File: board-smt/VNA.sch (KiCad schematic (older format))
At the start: 101 parts, among them J1 Conn_02x07_Odd_Even, J10 Conn_01x01, J11 Conn_01x01, J12 Conn_01x01, J13 Barrel_Jack, J14 Conn_01x01, J15 Conn_01x02, J16 Conn_01x01, J17 Conn_01x04, J18 Conn_01x01, J19 Conn_01x01, J2 Conn_Coaxial, J20 Conn_01x01, J21 Conn_01x01, J22 Conn_01x02, J24 USB_B, J3 Conn_01x01, J4 Conn_01x01, J5 Conn_01x01, J6 Conn_01x01, J7 Conn_01x01, J8 Conn_01x01, J9 Conn_Coaxial, Q3 S9018, SW1 SW_DPDT_x2, U1 SI5351A, U10 MT3608, U11 CN3052, U8 AMS1117-3V3, U9 78M05_TO252, Y1 27 MHz

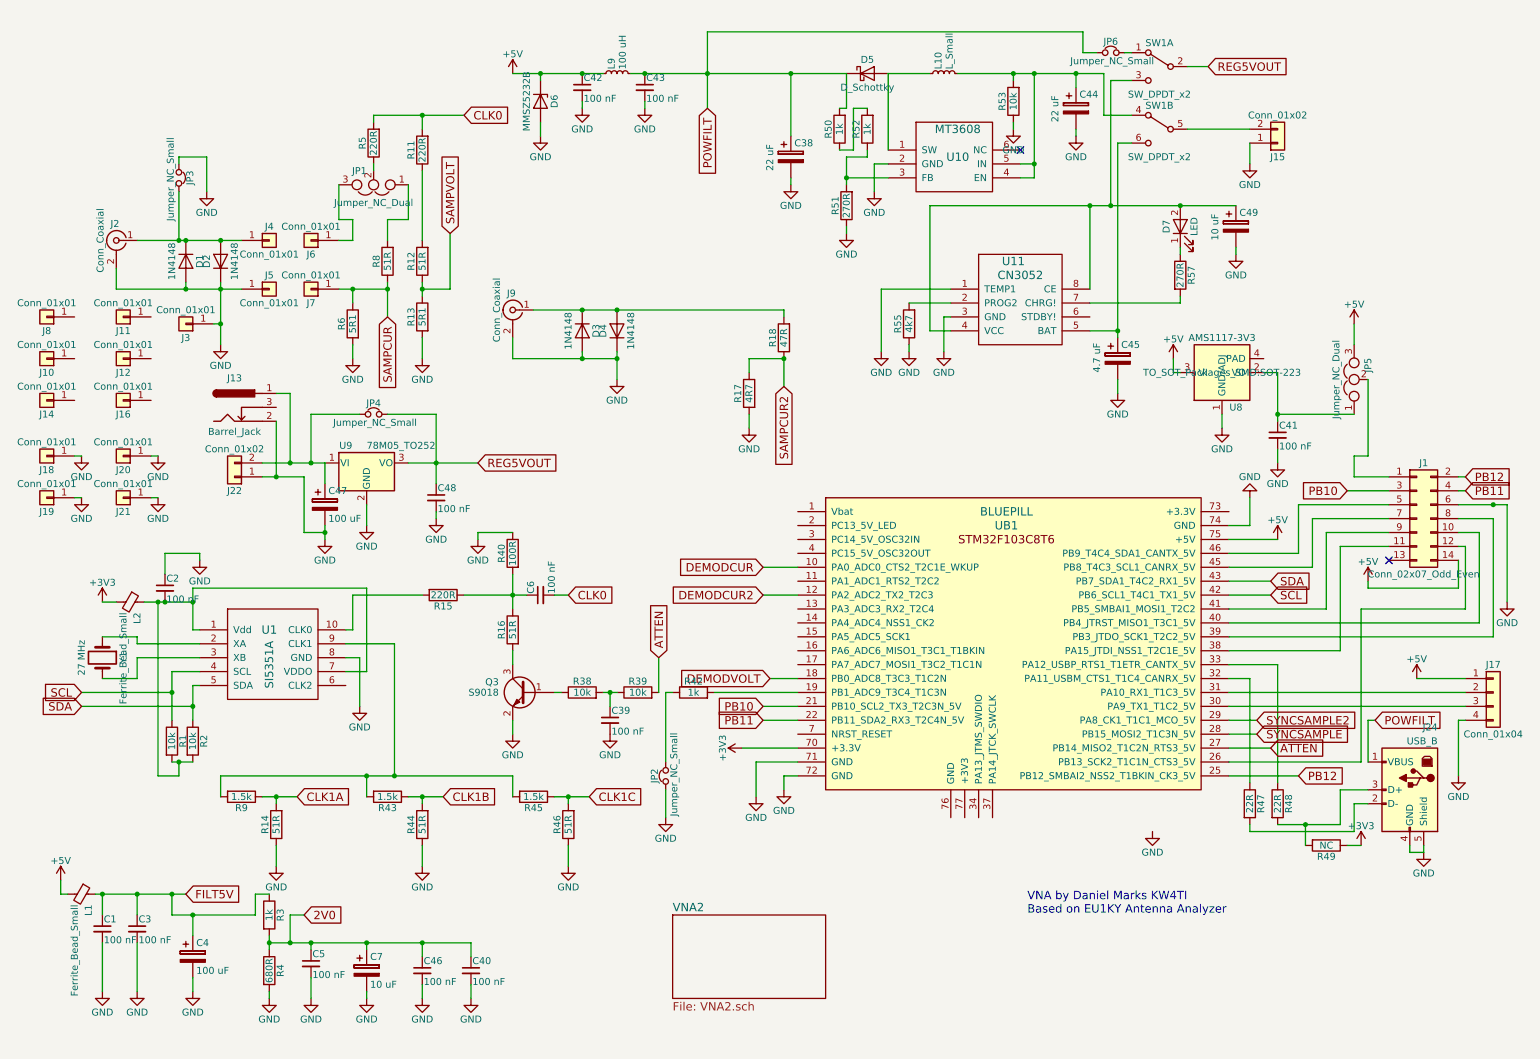
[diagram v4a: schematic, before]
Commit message: Added provision for separate SI5351A for LO signal
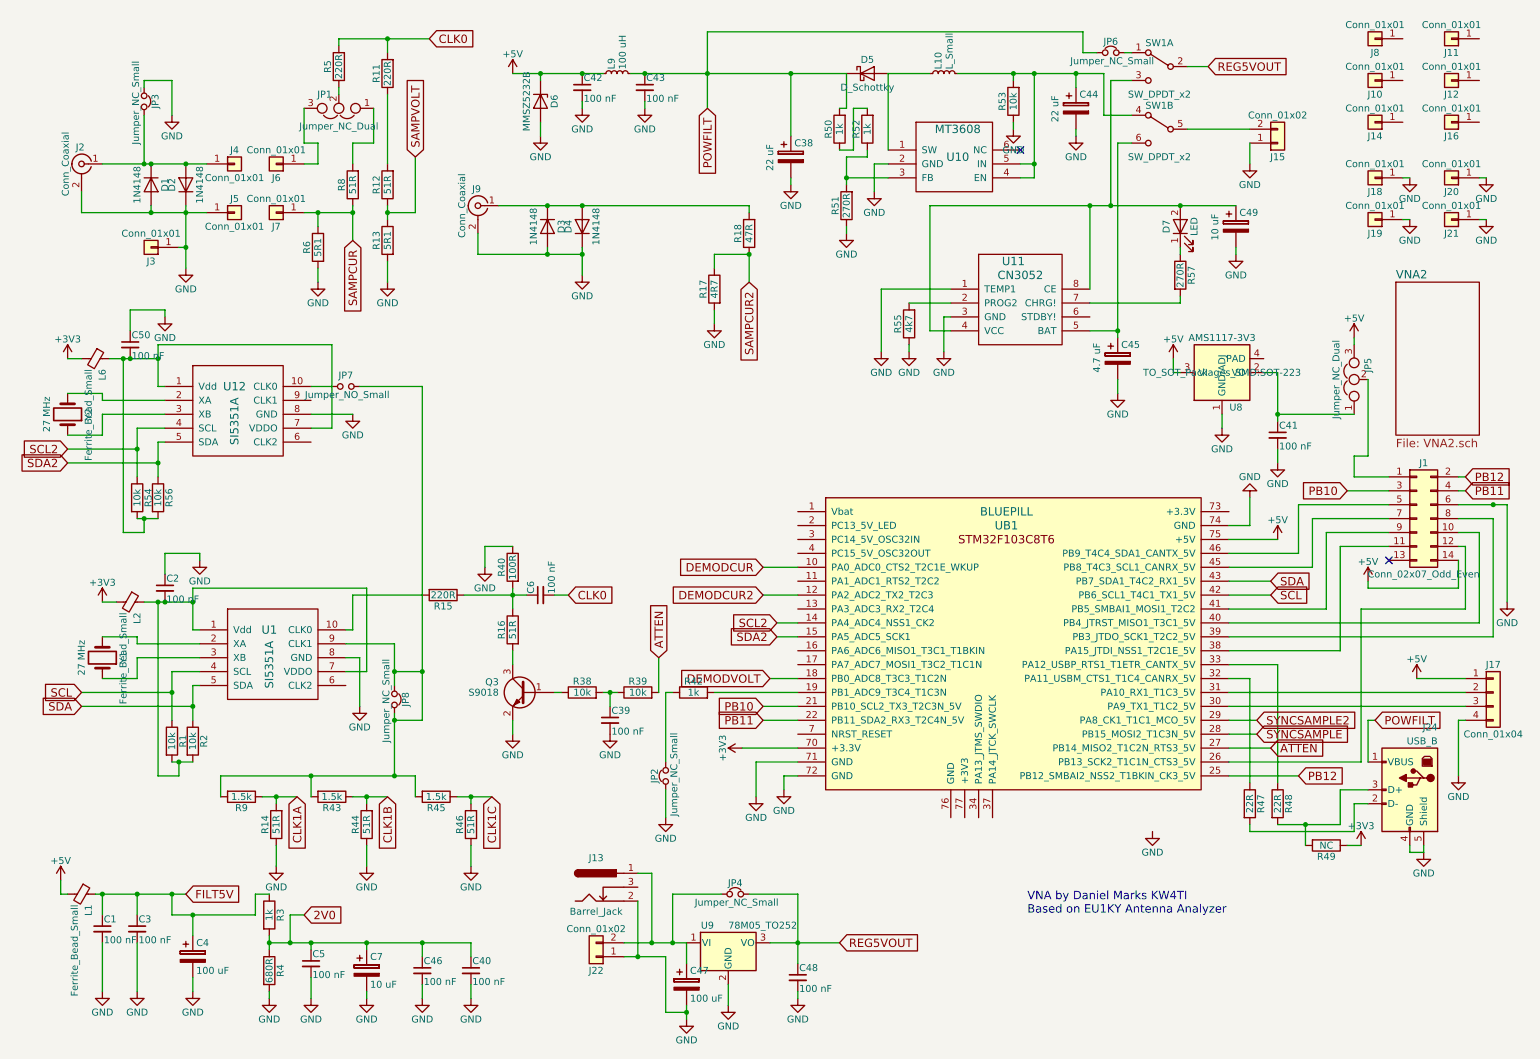
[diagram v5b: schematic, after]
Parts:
- added C50: 100 nF, Capacitors_SMD:C_0805_HandSoldering, symbol C_Small
- added JP7: Jumper_NO_Small, VNA:PAD_DEFAULT_OPEN, symbol Jumper_NO_Small
- added JP8: Jumper_NC_Small, VNA:PAD_DEFAULT_OPEN, symbol Jumper_NC_Small
- added L6: Ferrite_Bead_Small, Inductors_SMD:L_0805_HandSoldering, symbol Ferrite_Bead_Small
- added R54, R56: 10k, Resistors_SMD:R_0805_HandSoldering, symbol R
- added U12: SI5351A, Housings_SSOP:MSOP-10_3x3mm_Pitch0.5mm, symbol SI5351A
- added Y2: 27 MHz, Crystals:Crystal_SMD_3225-4pin_3.2x2.5mm_HandSoldering, symbol Crystal
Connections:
- net +3V3: now also L6.2
- net GND: now also C50.1, U12.8 (GND)
- net SCL2: now reaches UB1.14 (PA4_ADC4_NSS1_CK2)
- net SCL2: now also R54.1, U12.4 (SCL)
- net SDA2: now reaches UB1.15 (PA5_ADC5_SCK1)
- net SDA2: now also R56.1, U12.5 (SDA)
- net at U1.2 (XA): now also Y1.2; no longer Y1.1
- net at U1.3 (XB): now also Y1.1; no longer Y1.2
- net at R43.2, R45.2, R9.2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: now also JP7.2, JP8.1, JP8.2
- new net: C50.2, L6.1, R54.2, R56.2, U12.1 (Vdd), U12.7 (VDDO)
- new net: JP7.1, U12.10 (CLK0)
- new net: U12.2 (XA), Y2.2
- new net: U12.3 (XB), Y2.1
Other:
- moved on the sheet: C47, C48, D1, D2, D3, D4, J10, J11, J12, J13, J14, J16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

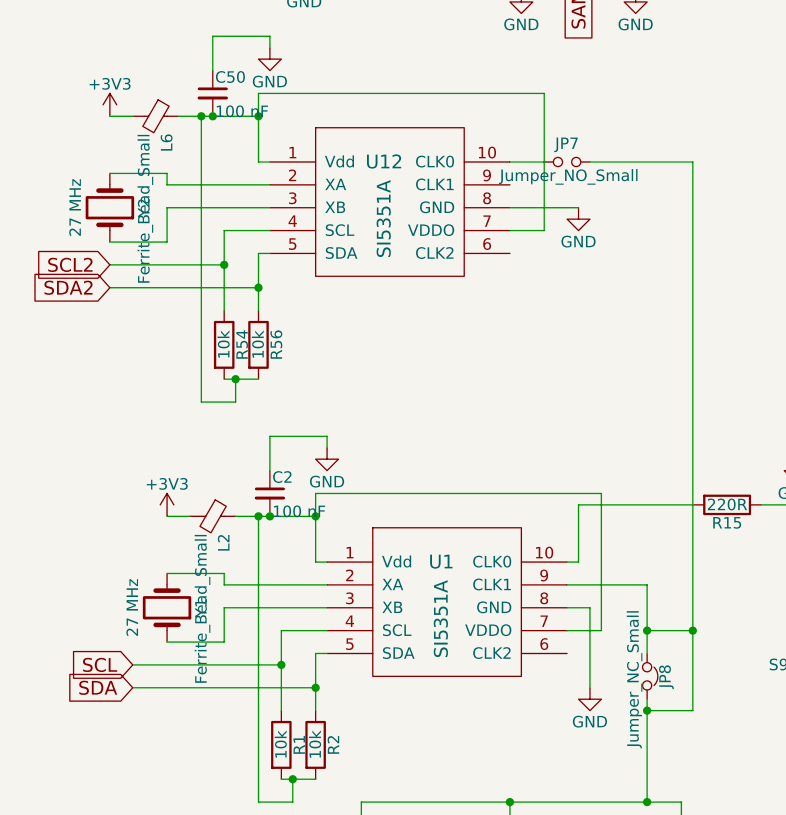
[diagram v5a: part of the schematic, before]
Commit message: Slaved the second SI5351A to the first SI5351A
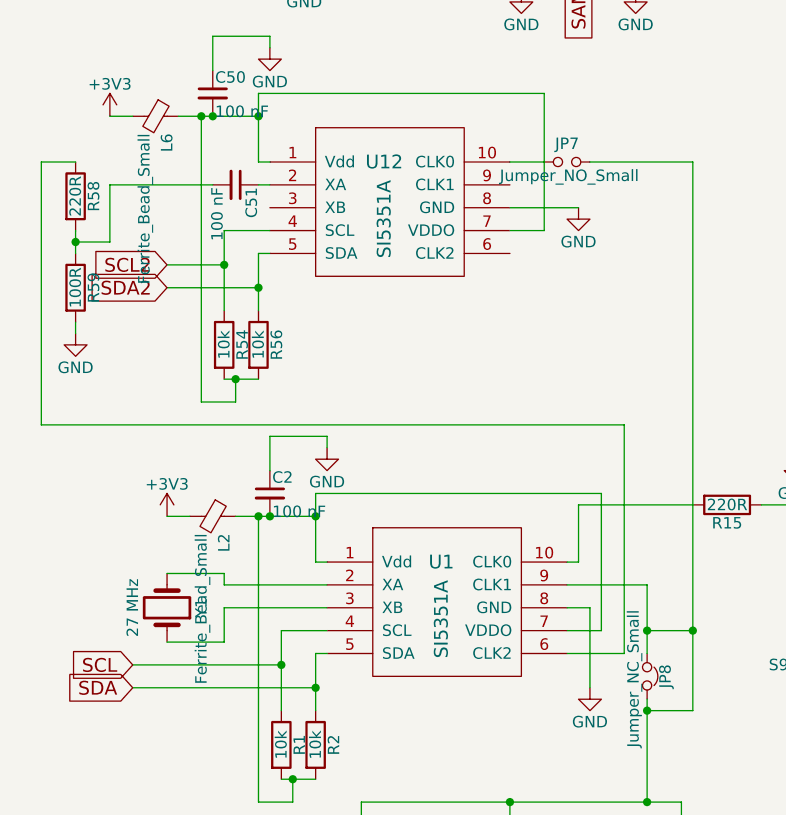
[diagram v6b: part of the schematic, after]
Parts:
- removed Y2: 27 MHz, Crystals:Crystal_SMD_3225-4pin_3.2x2.5mm_HandSoldering, symbol Crystal
- added C51: 100 nF, Capacitors_SMD:C_0805_HandSoldering, symbol C_Small
- added R58: 220R, Resistors_SMD:R_0805_HandSoldering, symbol R
- added R59: 100R, Resistors_SMD:R_0805_HandSoldering, symbol R
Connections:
- net GND: now also R59.2
- net at U1.6 (CLK2): now also R58.1
- net at U12.2 (XA): now also C51.1
- new net: C51.2, R58.2, R59.1

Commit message: JLCPCB order 2019-11-22
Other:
- moved on the sheet: JP7, R15

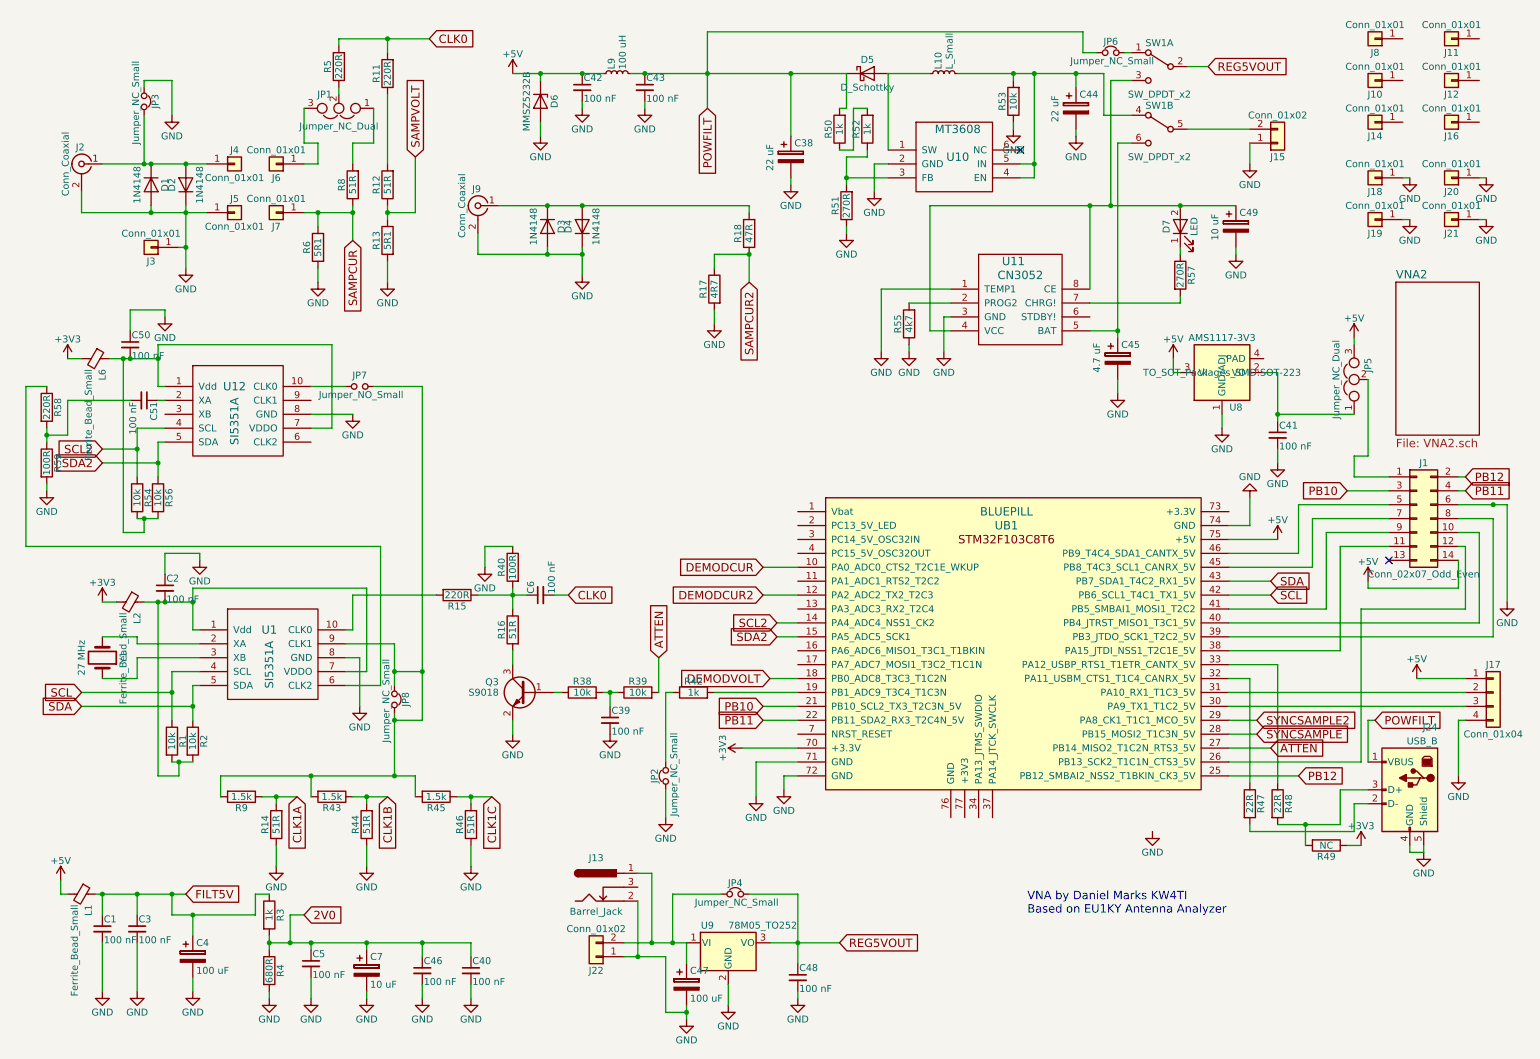
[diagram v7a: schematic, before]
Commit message: Fixed crystal pinout, added heatsink pad to CN3052A
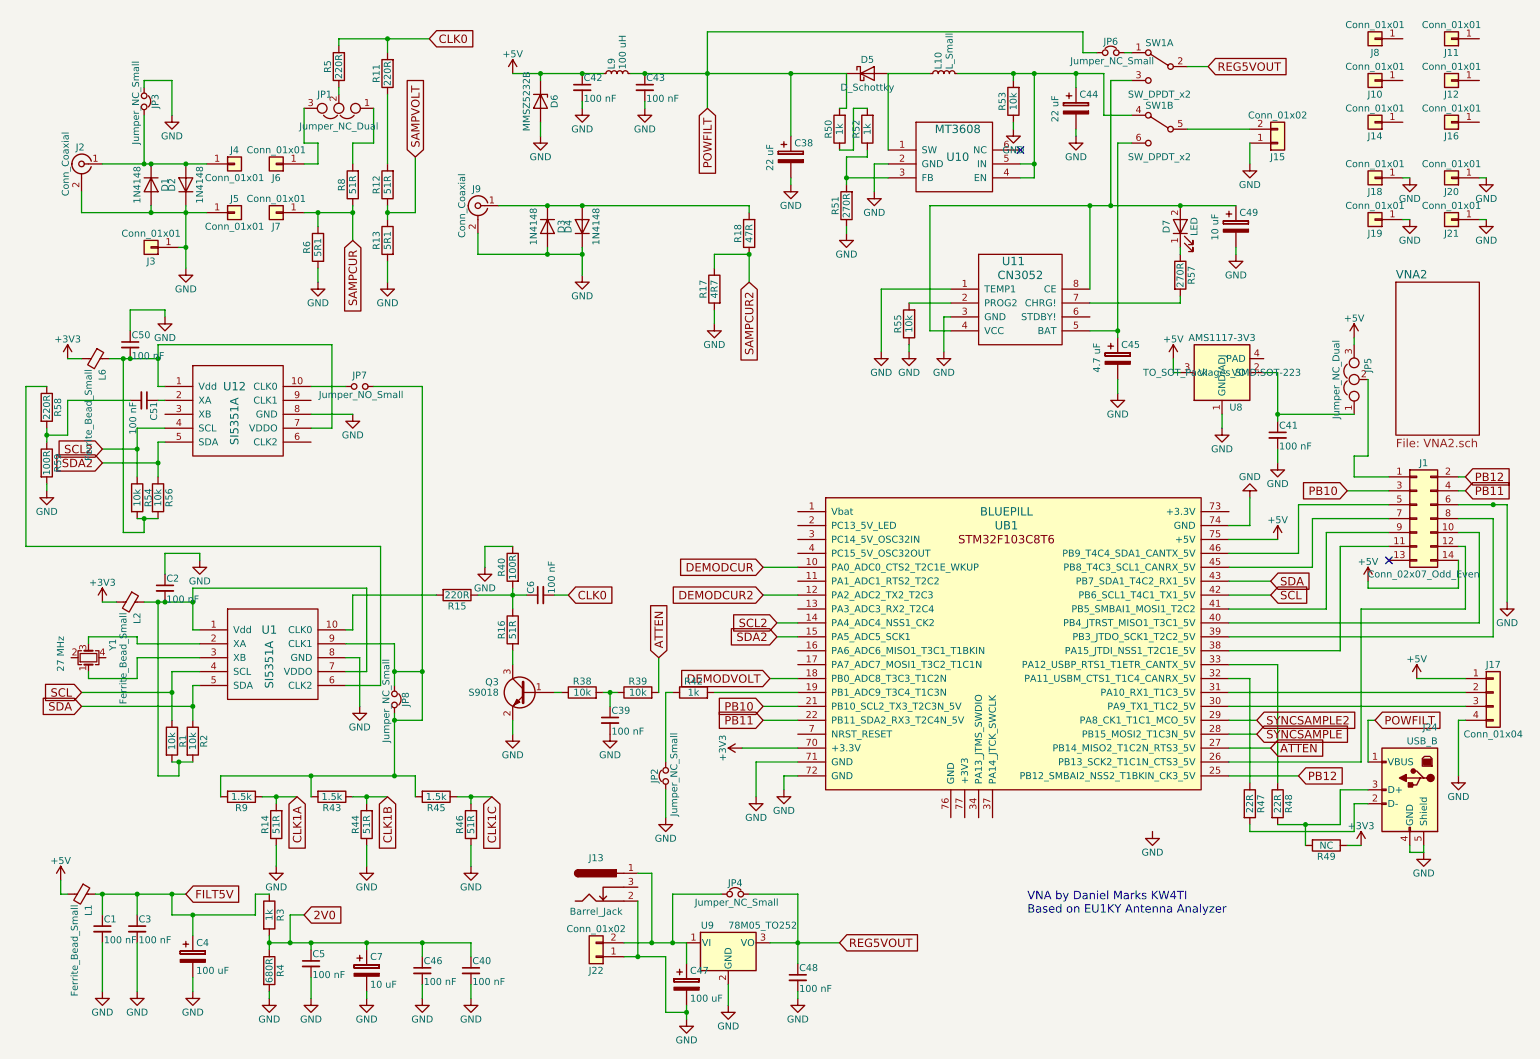
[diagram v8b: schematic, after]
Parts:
- removed Y1: 27 MHz, Crystals:Crystal_SMD_3225-4pin_3.2x2.5mm_HandSoldering, symbol Crystal
- added Y1: 27 MHz, symbol Crystal_GND24_Small
- R55: value 4k7 -> 10k
- U11: footprint Housings_SOIC:SOIC-8_3.9x4.9mm_Pitch1.27mm -> Housings_SOIC:TI_SO-PowerPAD-8
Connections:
- net at U1.2 (XA): now also Y1.3
- net at U1.3 (XB): now also Y1.1
